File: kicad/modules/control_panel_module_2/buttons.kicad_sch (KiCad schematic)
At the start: 9 parts, among them U1 ULN2004A

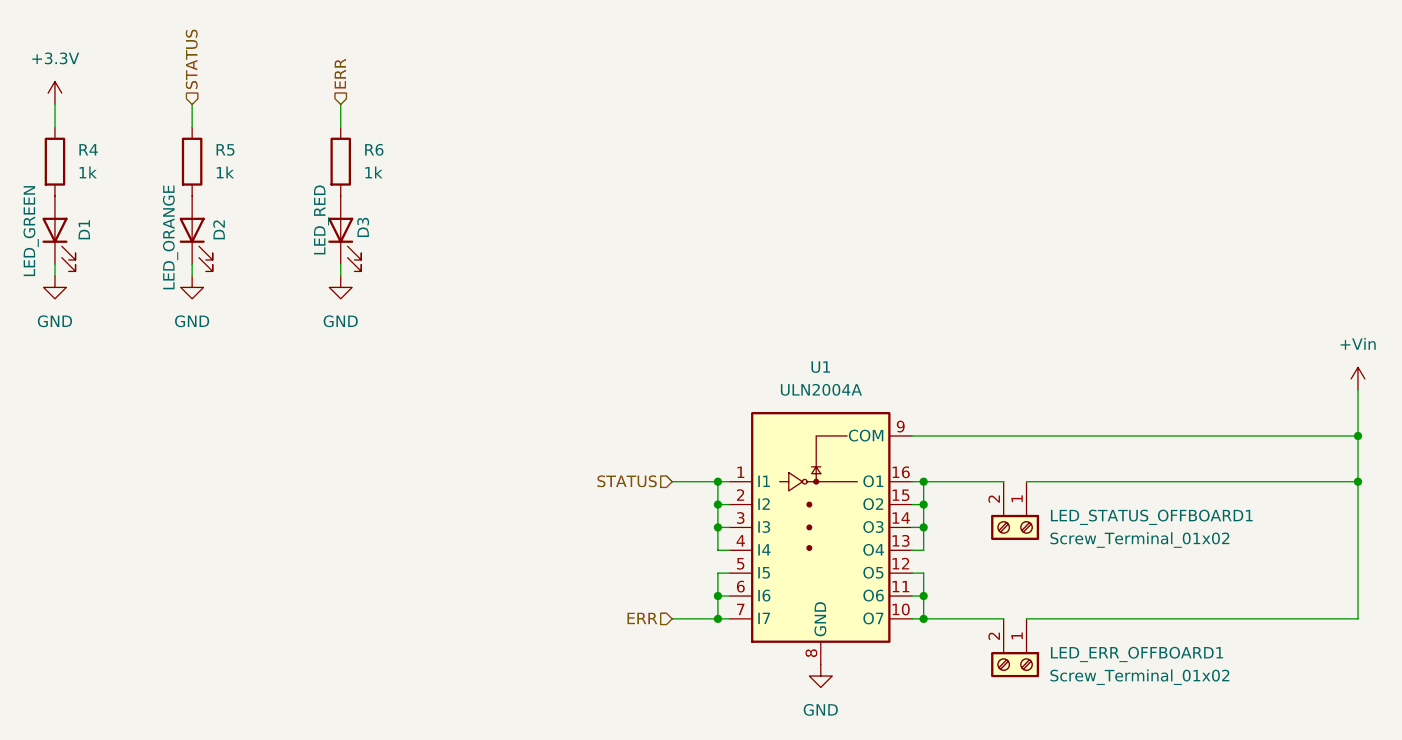
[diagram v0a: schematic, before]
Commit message: Connector for bigger current, control module 2
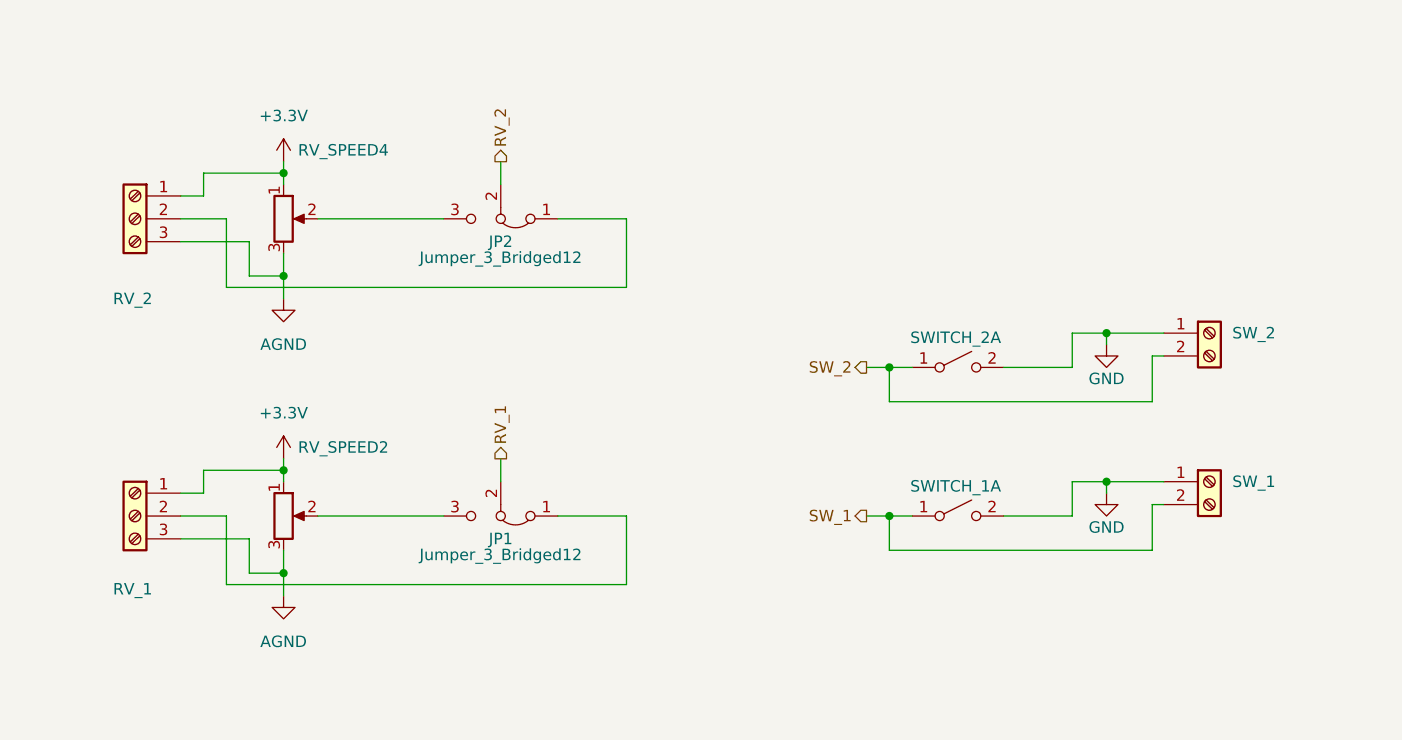
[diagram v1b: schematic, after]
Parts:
- removed D1: LED_GREEN, LED_SMD:LED_0603_1608Metric_Pad1.05x0.95mm_HandSolder, symbol Device:LED
- removed D2: LED_ORANGE, LED_SMD:LED_0603_1608Metric_Pad1.05x0.95mm_HandSolder, symbol Device:LED
- removed D3: LED_RED, LED_SMD:LED_0603_1608Metric_Pad1.05x0.95mm_HandSolder, symbol Device:LED
- removed LED_ERR_OFFBOARD1, LED_STATUS_OFFBOARD1: Screw_Terminal_01x02, TerminalBlock_MetzConnect:TerminalBlock_MetzConnect_Type101_RT01602HBWC_1x02_P5.08mm_Horizontal, symbol Connector:Screw_Terminal_01x02
- removed R4, R5, R6: 1k, Resistor_SMD:R_0603_1608Metric_Pad0.98x0.95mm_HandSolder, symbol Device:R
- removed U1: ULN2004A, Package_SO:SOIC-16W_5.3x10.2mm_P1.27mm, symbol Transistor_Array:ULN2004A
- added JP1, JP2: Jumper_3_Bridged12, Connector_PinHeader_2.54mm:PinHeader_1x03_P2.54mm_Vertical, symbol Jumper:Jumper_3_Bridged12
- added RV_1, RV_2: ~, TerminalBlock_MetzConnect:TerminalBlock_MetzConnect_Type101_RT01603HBWC_1x03_P5.08mm_Horizontal, symbol Connector:Screw_Terminal_01x03
- added RV_SPEED2, RV_SPEED4: 100k, Potentiometer_THT:Potentiometer_Alps_RK09K_Single_Vertical, symbol Device:R_Potentiometer
- added SWITCH_1, SWITCH_2: BTN, Button_Switch_SMD:SW_SPST_Omron_B3FS-105xP, symbol Switch:SW_DPST_x2
- added SW_1, SW_2: ~, TerminalBlock_MetzConnect:TerminalBlock_MetzConnect_Type101_RT01602HBWC_1x02_P5.08mm_Horizontal, symbol Connector:Screw_Terminal_01x02
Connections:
- net +3.3V: now also RV_1.1 (Pin_1), RV_2.1 (Pin_1), RV_SPEED2.1, RV_SPEED4.1
- net GND: now also SWITCH_1.2 (B), SWITCH_2.2 (B), SW_1.1 (Pin_1), SW_2.1 (Pin_1)
- new net: JP2.3 (B), RV_SPEED4.2
- new net: JP1.3 (B), RV_SPEED2.2
- new net: JP2.1 (A), RV_2.2 (Pin_2)
- new net: JP1.1 (A), RV_1.2 (Pin_2)
- new net AGND: RV_1.3 (Pin_3), RV_2.3 (Pin_3), RV_SPEED2.3, RV_SPEED4.3
- new net RV_1: JP1.2 (C)
- new net RV_2: JP2.2 (C)
- new net SW_1: SWITCH_1.1 (A), SW_1.2 (Pin_2)
- new net SW_2: SWITCH_2.1 (A), SW_2.2 (Pin_2)

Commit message: Add part numbers
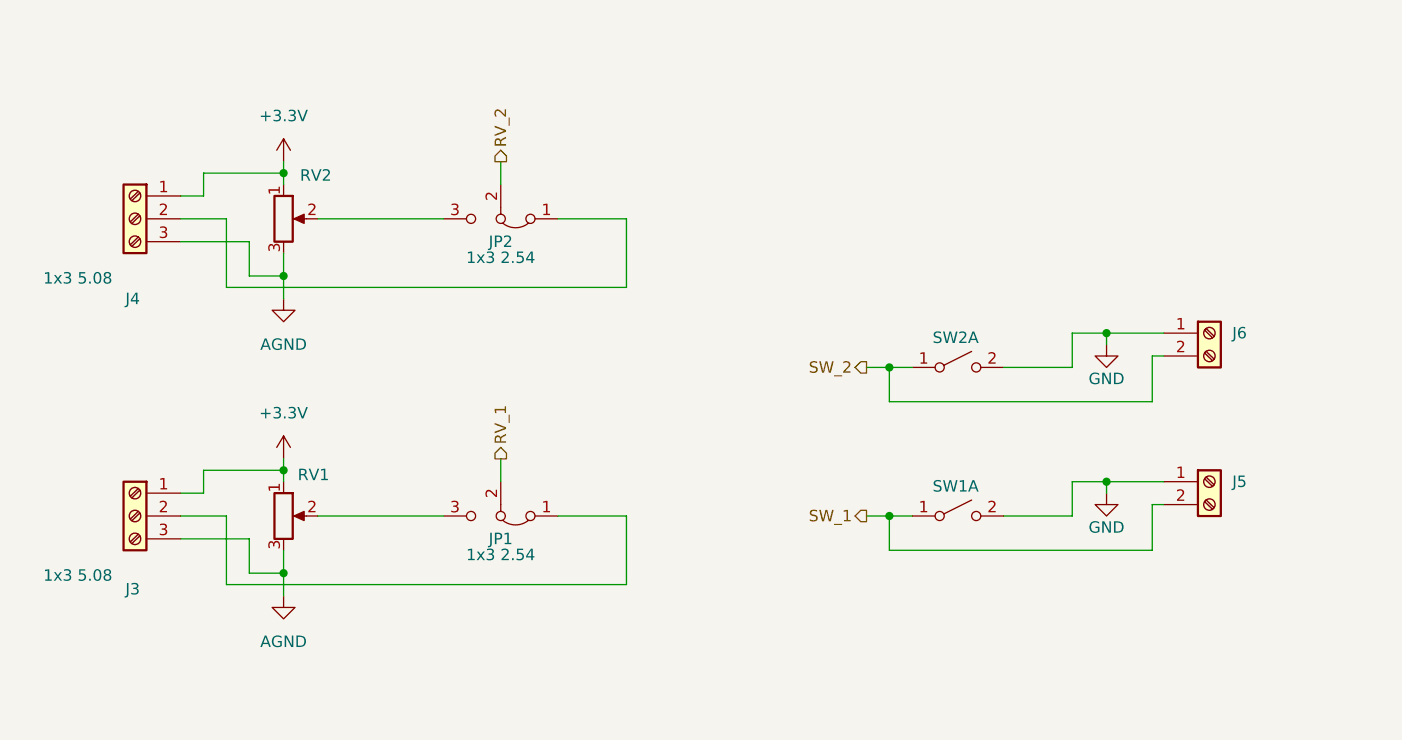
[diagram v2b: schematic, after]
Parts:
- J3: renamed from RV_1; value ~ -> 1x3 5.08
- J4: renamed from RV_2; value ~ -> 1x3 5.08
- J5: renamed from SW_1; value ~ -> 1x2 5.08
- J6: renamed from SW_2; value ~ -> 1x2 5.08
- JP1, JP2: value Jumper_3_Bridged12 -> 1x3 2.54; Manufacturer Part Number (none) -> 68000-420HLF; Mouser number (none) -> 649-68000-420HLF
- RV1: renamed from RV_SPEED2; Manufacturer Part Number (none) -> RK09D1130-F30-C0-B104
- RV2: renamed from RV_SPEED4; Manufacturer Part Number (none) -> RK09D1130-F30-C0-B104
- SW1: renamed from SWITCH_1; Manufacturer Part Number (none) -> B3FS-1095P
- SW2: renamed from SWITCH_2; Manufacturer Part Number (none) -> B3FS-1095P
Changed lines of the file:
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@@
 		(dnp no)
 		(fields_autoplaced yes)
-		(property "Reference" "SW_1"
+		(property "Reference" "J5"
 			(at 163.83 72.3899 0)
 			(effects
@@
 			)
 		)
-		(property "Value" "~"
+		(property "Value" "1x2 5.08"
 			(at 163.83 74.9299 0)
 			(effects
@@
 			)
 		)
-		(property "Description" "Generic screw terminal, single row, 01x02, script generated (kicad-library-utils/schlib/autogen/connector/)"
+		(property "Description" "CUSTOM"
 			(at 161.29 72.39 0)
 			(effects
@@
 			(project "control_panel_module"
 				(path "/01f48663-51d7-48f4-9aa9-9279c565a6cb/f1f09a98-6452-4cc9-9ea6-171d66ed561a"
-					(reference "SW_1")
+					(reference "J5")
 					(unit 1)
 				)
@@
 		(on_board yes)
 		(dnp no)
-		(property "Reference" "RV_SPEED4"
-			(at 70.104 35.56 0)
+		(property "Reference" "RV2"
+			(at 63.754 38.354 0)
 			(effects
 				(font
@@
 			)
 		)
-		(property "Description" ""
+		(property "Description" "CUSTOM"
 			(at 58.42 43.18 0)
 			(effects
@@
 			)
 		)
-		(property "Manufacturer Part Number" ""
+		(property "Manufacturer Part Number" "RK09D1130-F30-C0-B104"
 			(at 58.42 43.18 0)
 			(effects
@@
 			(project "control_panel_module_2"
 				(path "/01f48663-51d7-48f4-9aa9-9279c565a6cb/f1f09a98-6452-4cc9-9ea6-171d66ed561a"
-					(reference "RV_SPEED4")
+					(reference "RV2")
 					(unit 1)
 				)
@@
 		(on_board yes)
 		(dnp no)
-		(property "Reference" "RV_SPEED2"
-			(at 70.104 68.58 0)
+		(property "Reference" "RV1"
+			(at 63.5 71.628 0)
 			(effects
 				(font
@@
 			)
 		)
-		(property "Description" ""
+		(property "Description" "CUSTOM"
 			(at 58.42 76.2 0)
 			(effects
@@
 			)
 		)
-		(property "Manufacturer Part Number" ""
+		(property "Manufacturer Part Number" "RK09D1130-F30-C0-B104"
 			(at 58.42 76.2 0)
 			(effects
@@
 			(project "control_panel_module"
 				(path "/01f48663-51d7-48f4-9aa9-9279c565a6cb/f1f09a98-6452-4cc9-9ea6-171d66ed561a"
-					(reference "RV_SPEED2")
+					(reference "RV1")
 					(unit 1)
 				)
@@
 		(on_board yes)
 		(dnp no)
-		(property "Reference" "SWITCH_2"
+		(property "Reference" "SW2"
 			(at 133.096 56.388 0)
 			(effects
@@
 			)
 		)
-		(property "Description" ""
+		(property "Description" "CUSTOM"
 			(at 133.35 59.69 0)
 			(effects
@@
 			)
 		)
-		(property "Manufacturer Part Number" ""
+		(property "Manufacturer Part Number" "B3FS-1095P "
 			(at 133.35 59.69 0)
 			(effects
@@
 			(project "control_panel_module_2"
 				(path "/01f48663-51d7-48f4-9aa9-9279c565a6cb/f1f09a98-6452-4cc9-9ea6-171d66ed561a"
-					(reference "SWITCH_2")
+					(reference "SW2")
 					(unit 1)
 				)
@@
 			)
 		)
-		(property "Value" "Jumper_3_Bridged12"
+		(property "Value" "1x3 2.54"
 			(at 82.55 47.498 0)
 			(effects
@@
 			)
 		)
-		(property "Description" "Jumper, 3-pole, pins 1+2 closed/bridged"
+		(property "Description" "CUSTOM"
 			(at 82.55 43.18 0)
 			(effects
@@
 			)
 		)
-		(property "Manufacturer Part Number" ""
+		(property "Manufacturer Part Number" "68000-420HLF"
 			(at 82.55 43.18 0)
 			(effects
@@
 			)
 		)
-		(property "Mouser number" ""
+		(property "Mouser number" "649-68000-420HLF"
 			(at 82.55 43.18 0)
 			(effects
@@
 		(on_board yes)
 		(dnp no)
-		(property "Reference" "RV_1"
+		(property "Reference" "J3"
 			(at 41.656 84.328 0)
 			(effects
@@
 			)
 		)
-		(property "Value" "~"
+		(property "Value" "1x3 5.08"
 			(at 35.56 82.804 0)
 			(effects
@@
 			)
 		)
-		(property "Description" "Generic screw terminal, single row, 01x03, script generated (kicad-library-utils/schlib/autogen/connector/)"
+		(property "Description" "CUSTOM"
 			(at 41.91 76.2 0)
 			(effects
@@
 			(project "control_panel_module"
 				(path "/01f48663-51d7-48f4-9aa9-9279c565a6cb/f1f09a98-6452-4cc9-9ea6-171d66ed561a"
-					(reference "RV_1")
+					(reference "J3")
 					(unit 1)
 				)
@@
 			)
 		)
-		(property "Value" "Jumper_3_Bridged12"
+		(property "Value" "1x3 2.54"
 			(at 82.55 80.518 0)
 			(effects
@@
 			)
 		)
-		(property "Description" "Jumper, 3-pole, pins 1+2 closed/bridged"
+		(property "Description" "CUSTOM"
 			(at 82.55 76.2 0)
 			(effects
@@
 			)
 		)
-		(property "Manufacturer Part Number" ""
+		(property "Manufacturer Part Number" "68000-420HLF"
 			(at 82.55 76.2 0)
 			(effects
@@
 			)
 		)
-		(property "Mouser number" ""
+		(property "Mouser number" "649-68000-420HLF"
 			(at 82.55 76.2 0)
 			(effects
@@
 	)
 	(symbol
+		(lib_name "SW_DPST_x2_1")
 		(lib_id "Switch:SW_DPST_x2")
 		(at 133.35 76.2 0)
@@
 		(on_board yes)
 		(dnp no)
-		(property "Reference" "SWITCH_1"
+		(property "Reference" "SW1"
 			(at 133.096 72.898 0)
 			(effects
@@
 			)
 		)
-		(property "Description" ""
+		(property "Description" "CUSTOM"
 			(at 133.35 76.2 0)
 			(effects
@@
 			)
 		)
-		(property "Manufacturer Part Number" ""
+		(property "Manufacturer Part Number" "B3FS-1095P "
 			(at 133.35 76.2 0)
 			(effects
@@
 			(project "control_panel_module"
 				(path "/01f48663-51d7-48f4-9aa9-9279c565a6cb/f1f09a98-6452-4cc9-9ea6-171d66ed561a"
-					(reference "SWITCH_1")
+					(reference "SW1")
 					(unit 1)
 				)
@@
 		(dnp no)
 		(fields_autoplaced yes)
-		(property "Reference" "SW_2"
+		(property "Reference" "J6"
 			(at 163.83 55.8799 0)
 			(effects
@@
 			)
 		)
-		(property "Value" "~"
+		(property "Value" "1x2 5.08"
 			(at 163.83 58.4199 0)
 			(effects
@@
 			)
 		)
-		(property "Description" "Generic screw terminal, single row, 01x02, script generated (kicad-library-utils/schlib/autogen/connector/)"
+		(property "Description" "CUSTOM"
 			(at 161.29 55.88 0)
 			(effects
@@
 			(project "control_panel_module_2"
 				(path "/01f48663-51d7-48f4-9aa9-9279c565a6cb/f1f09a98-6452-4cc9-9ea6-171d66ed561a"
-					(reference "SW_2")
+					(reference "J6")
 					(unit 1)
 				)
@@
 		(on_board yes)
 		(dnp no)
-		(property "Reference" "RV_2"
+		(property "Reference" "J4"
 			(at 41.656 52.07 0)
 			(effects
@@
 			)
 		)
-		(property "Value" "~"
+		(property "Value" "1x3 5.08"
 			(at 35.56 49.784 0)
 			(effects
@@
 			)
 		)
-		(property "Description" "Generic screw terminal, single row, 01x03, script generated (kicad-library-utils/schlib/autogen/connector/)"
+		(property "Description" "CUSTOM"
 			(at 41.91 43.18 0)
 			(effects
@@
 			(project "control_panel_module_2"
 				(path "/01f48663-51d7-48f4-9aa9-9279c565a6cb/f1f09a98-6452-4cc9-9ea6-171d66ed561a"
-					(reference "RV_2")
-					(unit 1)
-				)
+					(reference "J4")
+					(unit 1)
+				)

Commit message: BOM with Ullmanna part numbers
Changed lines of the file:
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@@
 (kicad_sch
-	(version 20231120)
+	(version 20250114)
 	(generator "eeschema")
-	(generator_version "8.0")
+	(generator_version "9.0")
 	(paper "A5")
 	(junction
@@
 		(shape output)
 		(at 123.19 59.69 180)
-		(fields_autoplaced yes)
 		(effects
 			(font
@@
 		(shape output)
 		(at 82.55 69.85 90)
-		(fields_autoplaced yes)
 		(effects
 			(font
@@
 		(shape output)
 		(at 82.55 36.83 90)
-		(fields_autoplaced yes)
 		(effects
 			(font
@@
 		(shape output)
 		(at 123.19 76.2 180)
-		(fields_autoplaced yes)
 		(effects
 			(font
@@
 			)
 		)
+		(property "Ullmanna Part Number" ""
+			(at 161.29 72.39 0)
+			(effects
+				(font
+					(size 1.27 1.27)
+				)
+				(hide yes)
+			)
+		)
 		(pin "1"
 		)
@@
 			)
 		)
+		(property "Ullmanna Part Number" ""
+			(at 58.42 43.18 0)
+			(effects
+				(font
+					(size 1.27 1.27)
+				)
+				(hide yes)
+			)
+		)
 		(pin "3"
 		)
@@
 		)
 		(property "Mouser number" "688-RK09D1130F30B104"
+			(at 58.42 76.2 0)
+			(effects
+				(font
+					(size 1.27 1.27)
+				)
+				(hide yes)
+			)
+		)
+		(property "Ullmanna Part Number" ""
 			(at 58.42 76.2 0)
 			(effects
@@
 			)
 		)
+		(property "Ullmanna Part Number" ""
+			(at 133.35 59.69 0)
+			(effects
+				(font
+					(size 1.27 1.27)
+				)
+				(hide yes)
+			)
+		)
 		(pin "4"
 		)
@@
 		)
 		(property "Mouser number" "649-68000-420HLF"
+			(at 82.55 43.18 0)
+			(effects
+				(font
+					(size 1.27 1.27)
+				)
+				(hide yes)
+			)
+		)
+		(property "Ullmanna Part Number" ""
 			(at 82.55 43.18 0)
 			(effects
@@
 			)
 		)
+		(property "Ullmanna Part Number" ""
+			(at 41.91 76.2 0)
+			(effects
+				(font
+					(size 1.27 1.27)
+				)
+				(hide yes)
+			)
+		)
 		(pin "1"
 		)
@@
 		)
 		(property "Mouser number" "649-68000-420HLF"
+			(at 82.55 76.2 0)
+			(effects
+				(font
+					(size 1.27 1.27)
+				)
+				(hide yes)
+			)
+		)
+		(property "Ullmanna Part Number" ""
 			(at 82.55 76.2 0)
 			(effects
@@
 			)
 		)
+		(property "Ullmanna Part Number" ""
+			(at 133.35 76.2 0)
+			(effects
+				(font
+					(size 1.27 1.27)
+				)
+				(hide yes)
+			)
+		)
 		(pin "4"
 		)
@@
 			)
 		)
+		(property "Ullmanna Part Number" ""
+			(at 161.29 55.88 0)
+			(effects
+				(font
+					(size 1.27 1.27)
+				)
+				(hide yes)
+			)
+		)
 		(pin "1"
 		)
@@
 			(at 41.91 43.18 0)
 			(effects
+				(font
+					(size 1.27 1.27)
+				)
+				(hide yes)
+			)
+		)
+		(property "Ullmanna Part Number" ""
+			(at 41.91 43.18 0)
+			(effects
